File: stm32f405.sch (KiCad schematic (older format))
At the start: 17 parts, among them Q1 CRYSTAL_50X32, U1 STM32_STM32F10XRXT6

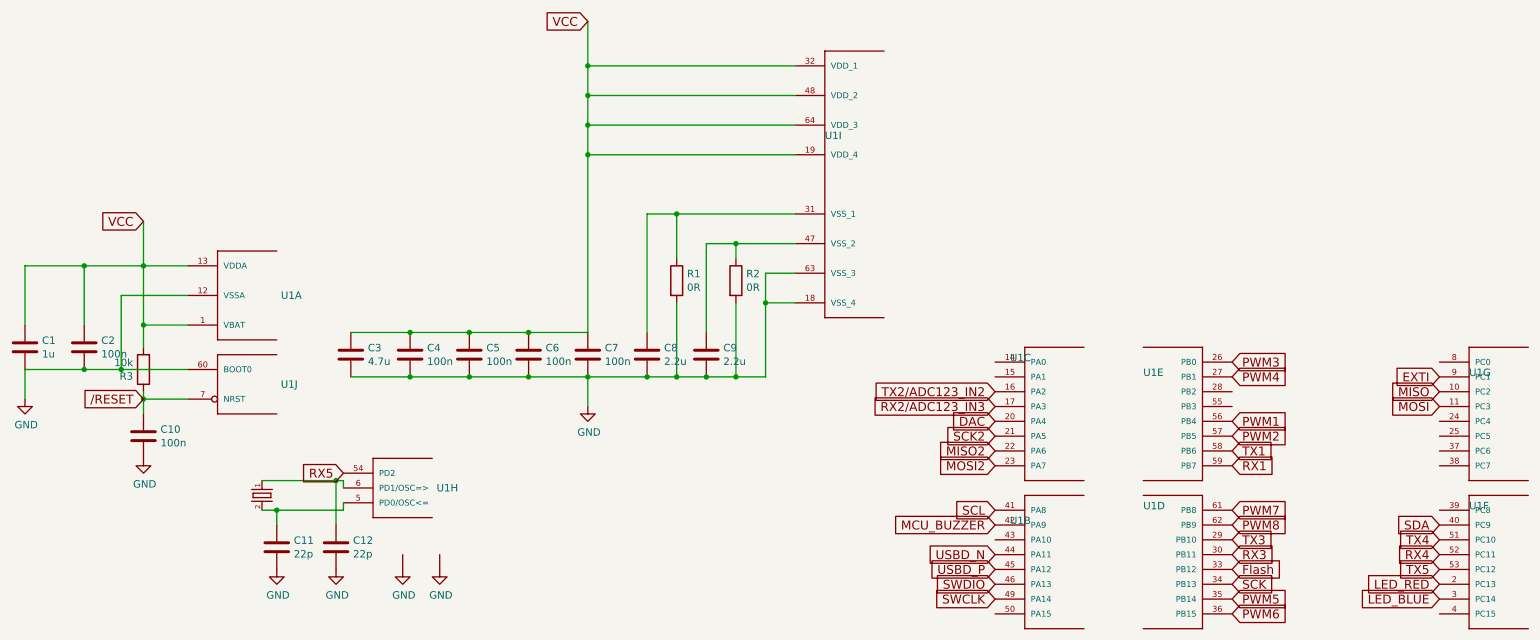
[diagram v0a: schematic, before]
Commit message: added i2c pullups, IMU int and USB sense
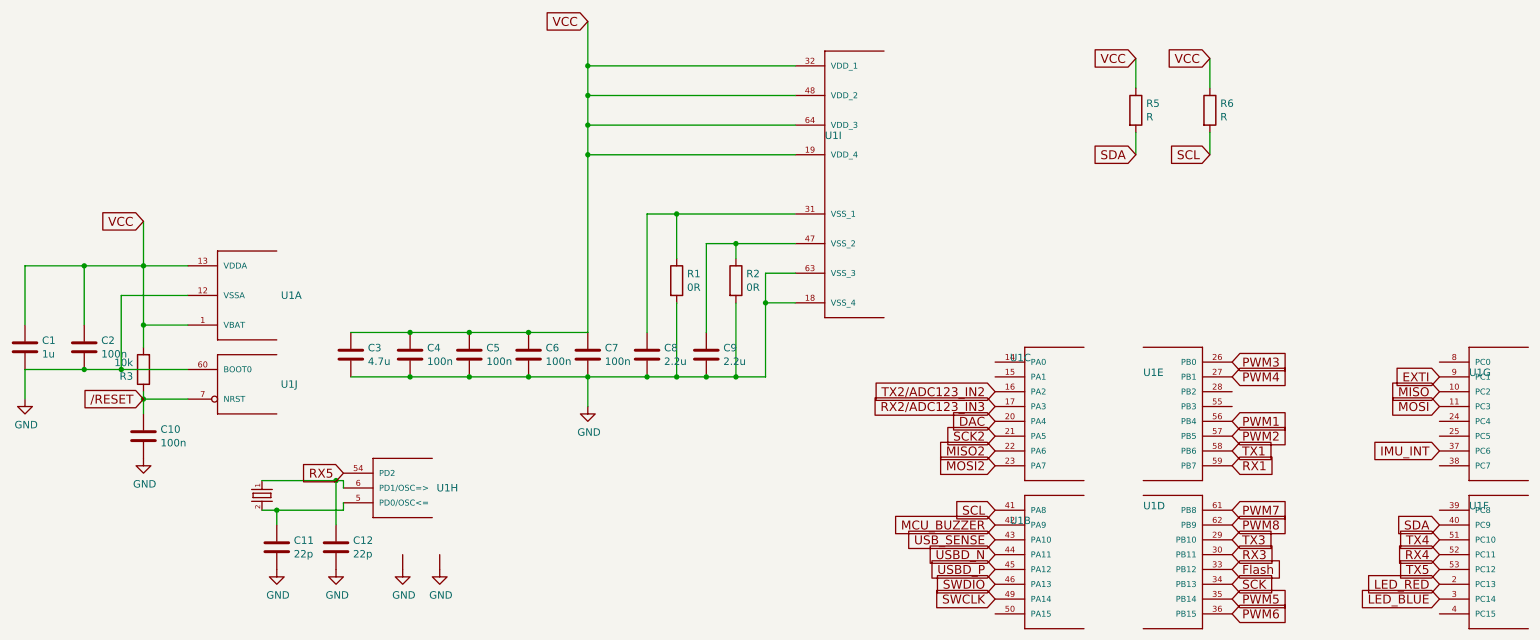
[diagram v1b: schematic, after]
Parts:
- added R5, R6: R, Resistors_SMD:R_0402, symbol R
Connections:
- net SCL: now also R6.2
- net SDA: now also R5.2
- net VCC: now also R5.1, R6.1
- net USB_SENSE: now reaches U1.43 (PA10)
- net IMU_INT: now reaches U1.37 (PC6)
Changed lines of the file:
@@
 LIBS:contrib
 LIBS:valves
-LIBS:minimal
 LIBS:alis_parts
 LIBS:stm32f4_lqfp64_mpu6050-cache
@@
 $EndComp
 $Comp
-L GND #PWR16
+L GND #PWR014
 U 1 1 569AE259
 P 4600 3750
-F 0 "#PWR16" H 4600 3500 50  0001 C CNN
+F 0 "#PWR014" H 4600 3500 50  0001 C CNN
 F 1 "GND" H 4608 3576 50  0000 C CNN
 F 2 "" H 4600 3750 50  0000 C CNN
@@
 $EndComp
 $Comp
-L GND #PWR15
+L GND #PWR015
 U 1 1 569AE27B
 P 800 3700
-F 0 "#PWR15" H 800 3450 50  0001 C CNN
+F 0 "#PWR015" H 800 3450 50  0001 C CNN
 F 1 "GND" H 808 3526 50  0000 C CNN
 F 2 "" H 800 3700 50  0000 C CNN
@@
 $EndComp
 $Comp
-L GND #PWR17
+L GND #PWR016
 U 1 1 569AE29F
 P 1600 4100
-F 0 "#PWR17" H 1600 3850 50  0001 C CNN
+F 0 "#PWR016" H 1600 3850 50  0001 C CNN
 F 1 "GND" H 1608 3926 50  0000 C CNN
 F 2 "" H 1600 4100 50  0000 C CNN
@@
 $EndComp
 $Comp
-L GND #PWR20
+L GND #PWR017
 U 1 1 569AE2B7
 P 3350 4850
-F 0 "#PWR20" H 3350 4600 50  0001 C CNN
+F 0 "#PWR017" H 3350 4600 50  0001 C CNN
 F 1 "GND" H 3358 4676 50  0000 C CNN
 F 2 "" H 3350 4850 50  0000 C CNN
@@
 $EndComp
 $Comp
-L GND #PWR21
+L GND #PWR018
 U 1 1 569AE2BD
 P 3600 4850
-F 0 "#PWR21" H 3600 4600 50  0001 C CNN
+F 0 "#PWR018" H 3600 4600 50  0001 C CNN
 F 1 "GND" H 3608 4676 50  0000 C CNN
 F 2 "" H 3600 4850 50  0000 C CNN
@@
 $EndComp
 $Comp
-L GND #PWR18
+L GND #PWR019
 U 1 1 569AE2D1
 P 2500 4850
-F 0 "#PWR18" H 2500 4600 50  0001 C CNN
+F 0 "#PWR019" H 2500 4600 50  0001 C CNN
 F 1 "GND" H 2508 4676 50  0000 C CNN
 F 2 "" H 2500 4850 50  0000 C CNN
@@
 $EndComp
 $Comp
-L GND #PWR19
+L GND #PWR020
 U 1 1 569AE2D7
 P 2900 4850
-F 0 "#PWR19" H 2900 4600 50  0001 C CNN
+F 0 "#PWR020" H 2900 4600 50  0001 C CNN
 F 1 "GND" H 2908 4676 50  0000 C CNN
 F 2 "" H 2900 4850 50  0000 C CNN
@@
 Text GLabel 10350 5050 0    60   Input ~ 0
 LED_BLUE
+$Comp
+L R R5
+U 1 1 57052683
+P 8300 1750
+F 0 "R5" H 8370 1796 50  0000 L CNN
+F 1 "R" H 8370 1705 50  0000 L CNN
+F 2 "Resistors_SMD:R_0402" V 8230 1750 50  0001 C CNN
+F 3 "" H 8300 1750 50  0000 C CNN
+	1    8300 1750
+	1    0    0    -1
+$EndComp
+$Comp
+L R R6
+U 1 1 570526F3
+P 8800 1750
+F 0 "R6" H 8870 1796 50  0000 L CNN
+F 1 "R" H 8870 1705 50  0000 L CNN
+F 2 "Resistors_SMD:R_0402" V 8730 1750 50  0001 C CNN
+F 3 "" H 8800 1750 50  0000 C CNN
+	1    8800 1750
+	1    0    0    -1
+$EndComp
+Text GLabel 8300 2050 0    60   Input ~ 0
+SDA
+Text GLabel 8800 2050 0    60   Input ~ 0
+SCL
+Text GLabel 8300 1400 0    60   Input ~ 0
+VCC
+Text GLabel 8800 1400 0    60   Input ~ 0
+VCC
+Wire Wire Line
+	8300 1400 8300 1600
+Wire Wire Line
+	8800 1400 8800 1600
+Wire Wire Line
+	8800 2050 8800 1900
+Wire Wire Line
+	8300 2050 8300 1900
+Text GLabel 10350 4050 0    60   Input ~ 0
+IMU_INT
+Text GLabel 7350 4650 0    60   Input ~ 0
+USB_SENSE
 $EndSCHEMATC
